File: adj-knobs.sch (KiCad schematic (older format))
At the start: 64 parts

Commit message: Initial PCB routed
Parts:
- removed C? (x2): 100nF, symbol Device:C_Small
- removed Q? (x4): 2N3904, Package_TO_SOT_THT:TO-92_Inline, symbol Transistor_BJT:2N3904
- removed U? (x14): 74HC14, symbol 74xx:74HC14
- added Q11, Q12, Q13, Q14: MMBT3904, Package_TO_SOT_SMD:SOT-23, symbol Transistor_BJT:MMBT3904
- added R70, R71, R72, R73: 1K, Resistor_SMD:R_0603_1608Metric_Pad0.98x0.95mm_HandSolder, symbol Device:R_Small
- added U1, U16, U17, U18, U19, U20: 74LVC2G14, Package_TO_SOT_SMD:SOT-23-6_Handsoldering, symbol 74xGxx:74LVC2G14
- C34, C35, C36, C37, C38, C39, C40, C41, C42, C43, C44, C45: renamed from C?; footprint (none) -> Capacitor_SMD:C_0603_1608Metric_Pad1.08x0.95mm_HandSolder
- R29, R30, R31, R32, R33, R35, R36, R37, R39, R40, R41, R43, R44, R45, R46, R47, R49, R50, R51, R52: renamed from R?; footprint (none) -> Resistor_SMD:R_0603_1608Metric_Pad0.98x0.95mm_HandSolder
- R34, R38, R42, R48: renamed from R?; value R_Small -> 1K; footprint (none) -> Resistor_SMD:R_0603_1608Metric_Pad0.98x0.95mm_HandSolder
- SW29, SW31, SW33, SW35: renamed from SW?; footprint (none) -> TL-1240:TL-1240
- SW30, SW32, SW34, SW36: renamed from SW?; footprint (none) -> Rotary_Encoder:RotaryEncoder_Alps_EC11E_Vertical_H20mm
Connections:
- wire segments 124 -> 120
- no-connect marks 8 -> 4

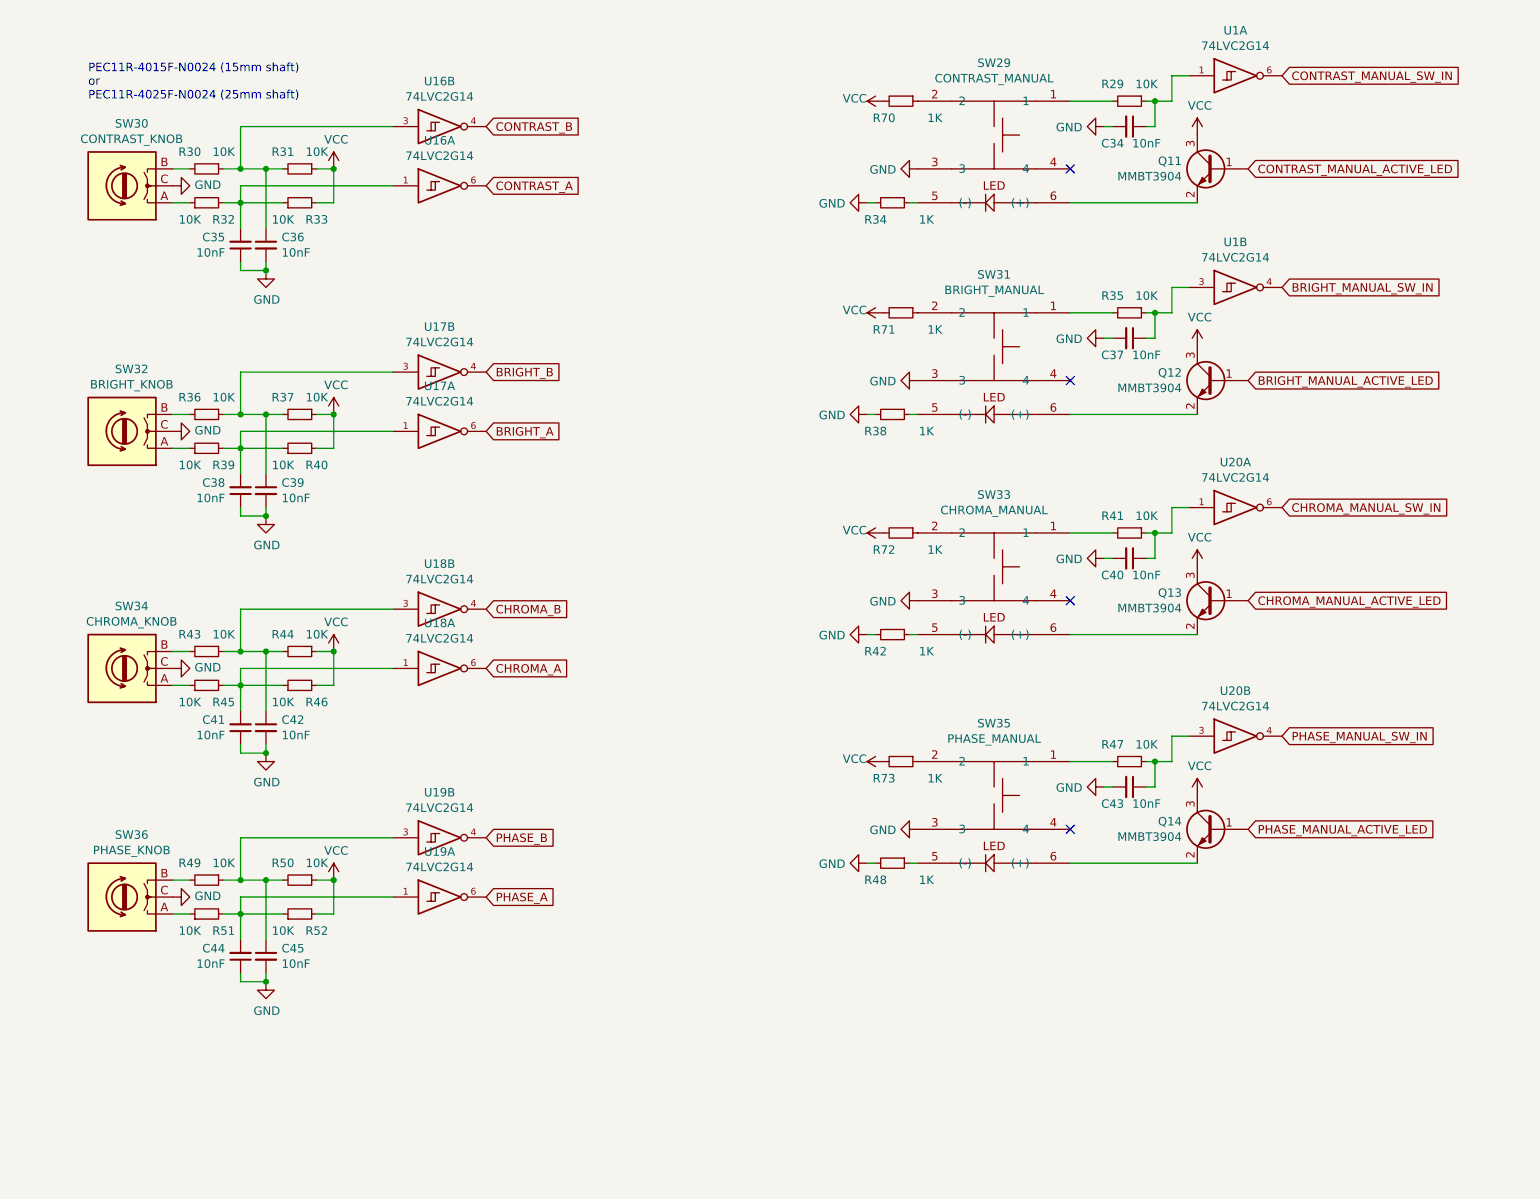
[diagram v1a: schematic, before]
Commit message: A bunch of changes, full duplex 422
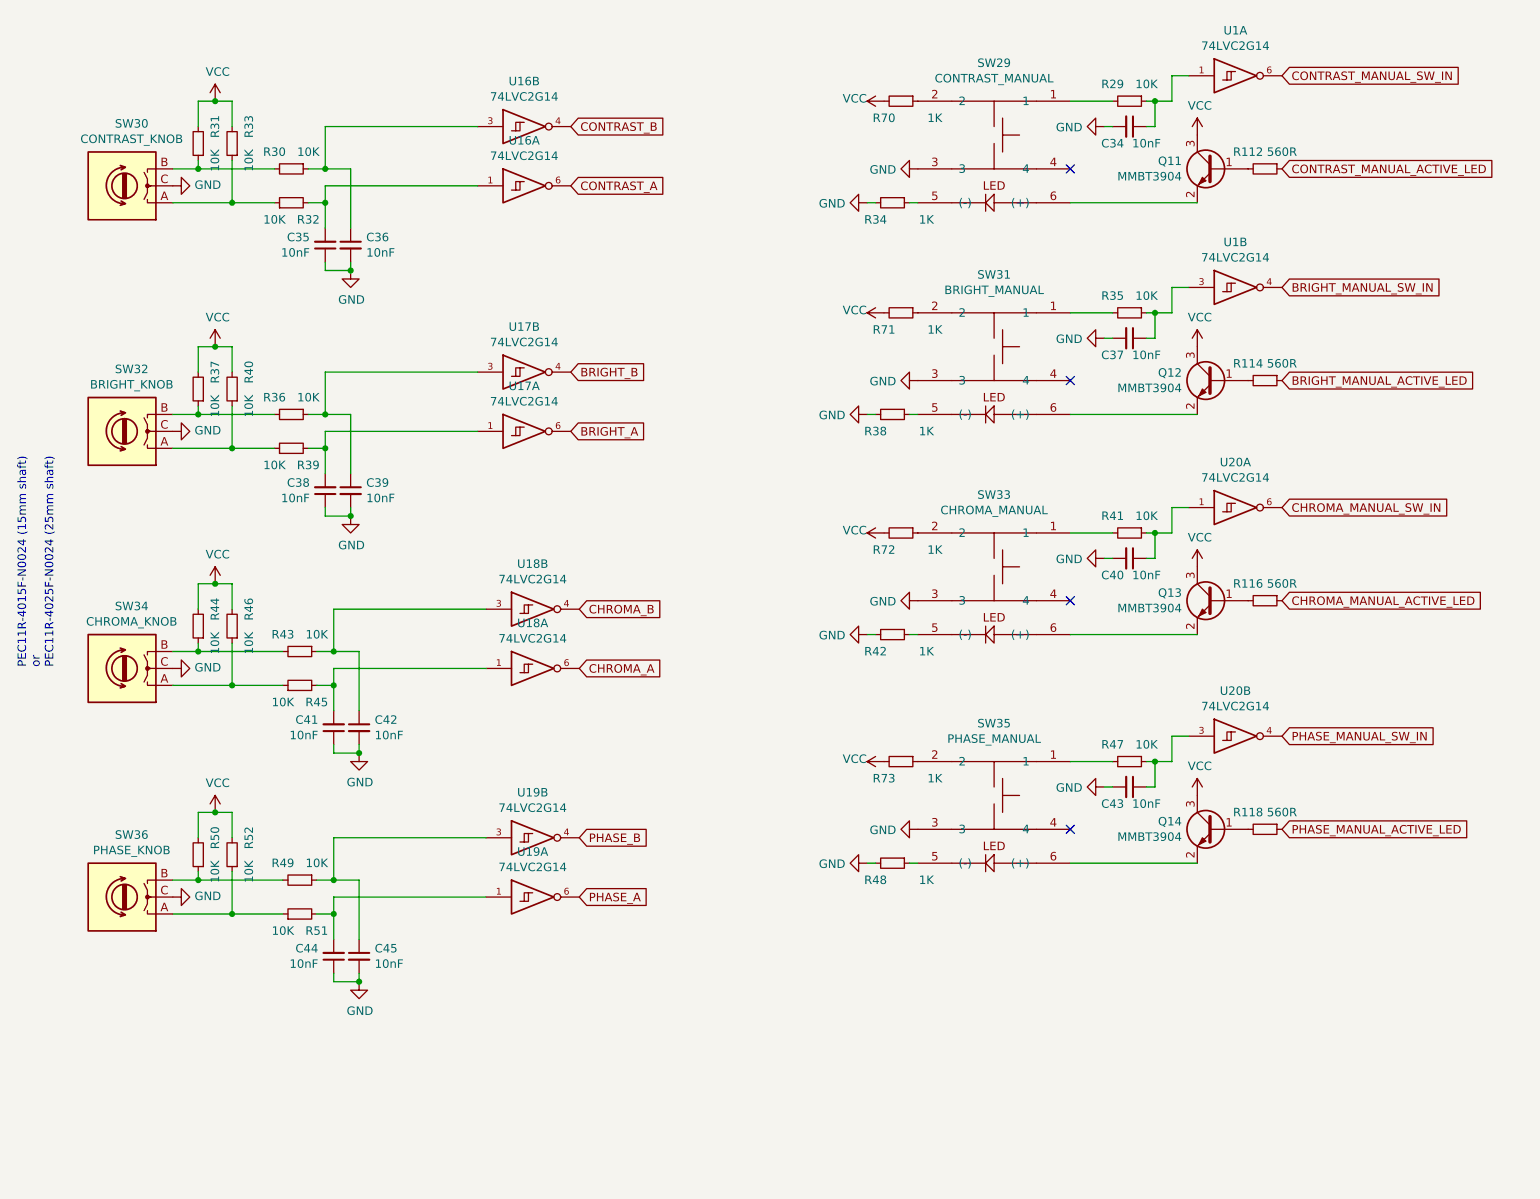
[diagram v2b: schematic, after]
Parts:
- added R112, R114, R116, R118: 560R, Resistor_SMD:R_0603_1608Metric_Pad0.98x0.95mm_HandSolder, symbol Device:R_Small
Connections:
- net BRIGHT_MANUAL_ACTIVE_LED: now also R114.1; no longer Q12.1 (B)
- net CHROMA_MANUAL_ACTIVE_LED: now also R116.1; no longer Q13.1 (B)
- net CONTRAST_MANUAL_ACTIVE_LED: now also R112.1; no longer Q11.1 (B)
- net PHASE_MANUAL_ACTIVE_LED: now also R118.1; no longer Q14.1 (B)
- net VCC: now also R31.2, R37.2, R44.2, R50.2; no longer R31.1, R37.1, R44.1, R50.1
- net at C45.1, R49.1, U19.3: no longer R50.2
- net at C44.2, R51.2, U19.1: no longer R52.1
- net at C42.1, R43.1, U18.3: no longer R44.2
- net at C41.2, R45.2, U18.1: no longer R46.1
- net at C39.1, R36.1, U17.3: no longer R37.2
- net at C38.2, R39.2, U17.1: no longer R40.1
- net at C36.1, R30.1, U16.3: no longer R31.2
- net at C35.2, R32.2, U16.1: no longer R33.1
- net at R32.1, SW30.A: now also R33.1
- net at R30.2, SW30.B: now also R31.1
- net at R39.1, SW32.A: now also R40.1
- net at R36.2, SW32.B: now also R37.1
- net at R45.1, SW34.A: now also R46.1
- net at R43.2, SW34.B: now also R44.1
- net at R51.1, SW36.A: now also R52.1
- net at R49.2, SW36.B: now also R50.1
- new net: Q11.1 (B), R112.2
- new net: Q12.1 (B), R114.2
- new net: Q13.1 (B), R116.2
- new net: Q14.1 (B), R118.2
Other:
- moved on the sheet: C35, C36, C38, C39, C41, C42, C44, C45, R30, R31, R32, R33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

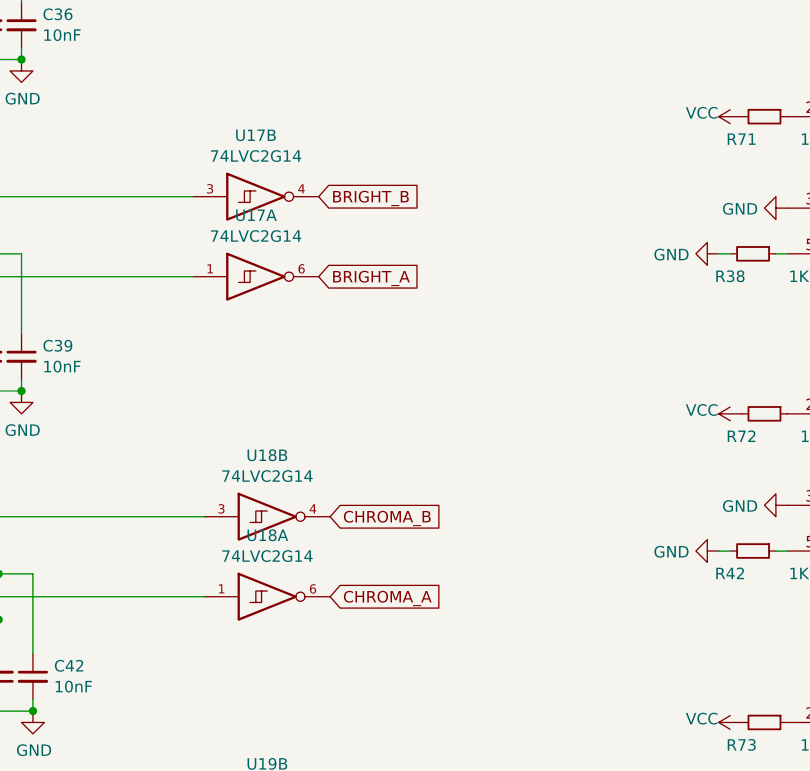
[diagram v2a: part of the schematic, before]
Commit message: Fixed switch footprints and encoder resistors
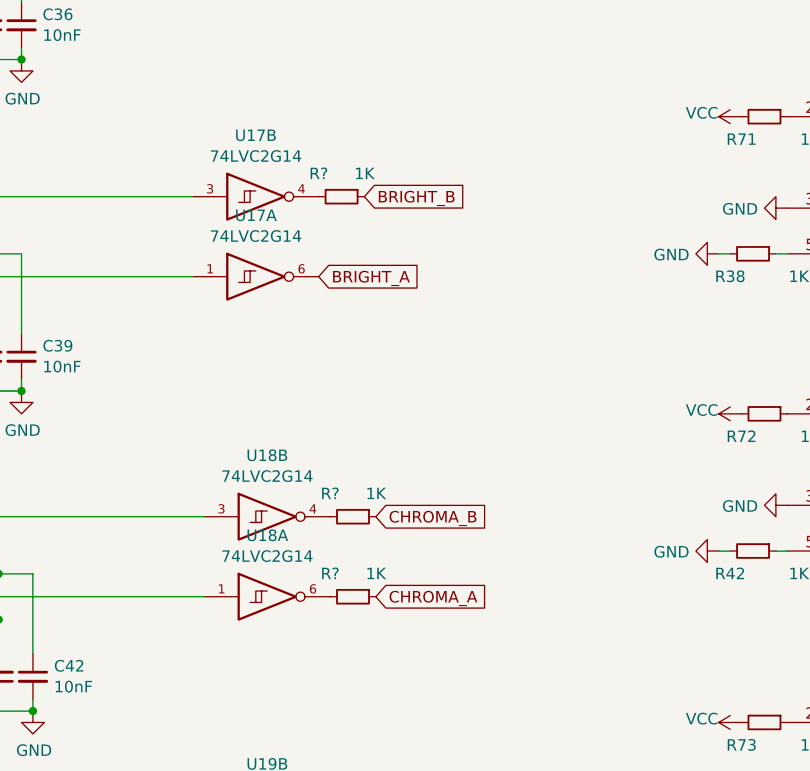
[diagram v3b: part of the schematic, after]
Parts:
- added R? (x3): 1K, Resistor_SMD:R_0603_1608Metric_Pad0.98x0.95mm_HandSolder, symbol Device:R_Small
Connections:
- net BRIGHT_B: now also R?.1; no longer U17.4
- net CHROMA_A: now also R?.1; no longer U18.6
- net CHROMA_B: now also R?.1; no longer U18.4
- new net: R?.2, U18.4
- new net: R?.2, U18.6
- new net: R?.2, U17.4
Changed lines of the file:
@@
 Text GLabel 4000 3200 2    50   Input ~ 0
 BRIGHT_A
-Text GLabel 4000 2850 2    50   Input ~ 0
+Text GLabel 4200 2850 2    50   Input ~ 0
 BRIGHT_B
 $Comp
@@
 Wire Wire Line
 	2600 4500 2750 4500
-Text GLabel 4050 4600 2    50   Input ~ 0
+Text GLabel 4250 4600 2    50   Input ~ 0
 CHROMA_A
-Text GLabel 4050 4250 2    50   Input ~ 0
+Text GLabel 4250 4250 2    50   Input ~ 0
 CHROMA_B
 $Comp
@@
 Wire Wire Line
 	1900 5450 2000 5450
+$Comp
+L Device:R_Small R?
+U 1 1 61CFAEB2
+P 4150 4250
+F 0 "R?" V 4050 4150 50  0000 C CNN
+F 1 "1K" V 4050 4350 50  0000 C CNN
+F 2 "Resistor_SMD:R_0603_1608Metric_Pad0.98x0.95mm_HandSolder" H 4150 4250 50  0001 C CNN
+F 3 "~" H 4150 4250 50  0001 C CNN
+	1    4150 4250
+	0    1    1    0
+$EndComp
+$Comp
+L Device:R_Small R?
+U 1 1 61D15885
+P 4150 4600
+F 0 "R?" V 4050 4500 50  0000 C CNN
+F 1 "1K" V 4050 4700 50  0000 C CNN
+F 2 "Resistor_SMD:R_0603_1608Metric_Pad0.98x0.95mm_HandSolder" H 4150 4600 50  0001 C CNN
+F 3 "~" H 4150 4600 50  0001 C CNN
+	1    4150 4600
+	0    1    1    0
+$EndComp
+$Comp
+L Device:R_Small R?
+U 1 1 61D279DB
+P 4100 2850
+F 0 "R?" V 4000 2750 50  0000 C CNN
+F 1 "1K" V 4000 2950 50  0000 C CNN
+F 2 "Resistor_SMD:R_0603_1608Metric_Pad0.98x0.95mm_HandSolder" H 4100 2850 50  0001 C CNN
+F 3 "~" H 4100 2850 50  0001 C CNN
+	1    4100 2850
+	0    1    1    0
+$EndComp
 $EndSCHEMATC

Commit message: 3D files and minor stuff
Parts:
- gave numbers to parts that had none: 3
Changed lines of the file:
@@
 encoding utf-8
 Sheet 5 6
-Title ""
+Title "BKM-10Rlternative"
 Date ""
 Rev ""
-Comp ""
+Comp "www.immerhax.com"
 Comment1 ""
 Comment2 ""
@@
 	1900 5450 2000 5450
 $Comp
-L Device:R_Small R?
+L Device:R_Small R113
 U 1 1 61CFAEB2
 P 4150 4250
-F 0 "R?" V 4050 4150 50  0000 C CNN
+F 0 "R113" V 4050 4150 50  0000 C CNN
 F 1 "1K" V 4050 4350 50  0000 C CNN
 F 2 "Resistor_SMD:R_0603_1608Metric_Pad0.98x0.95mm_HandSolder" H 4150 4250 50  0001 C CNN
@@
 $EndComp
 $Comp
-L Device:R_Small R?
+L Device:R_Small R115
 U 1 1 61D15885
 P 4150 4600
-F 0 "R?" V 4050 4500 50  0000 C CNN
+F 0 "R115" V 4050 4500 50  0000 C CNN
 F 1 "1K" V 4050 4700 50  0000 C CNN
 F 2 "Resistor_SMD:R_0603_1608Metric_Pad0.98x0.95mm_HandSolder" H 4150 4600 50  0001 C CNN
@@
 $EndComp
 $Comp
-L Device:R_Small R?
+L Device:R_Small R111
 U 1 1 61D279DB
 P 4100 2850
-F 0 "R?" V 4000 2750 50  0000 C CNN
+F 0 "R111" V 4000 2750 50  0000 C CNN
 F 1 "1K" V 4000 2950 50  0000 C CNN
 F 2 "Resistor_SMD:R_0603_1608Metric_Pad0.98x0.95mm_HandSolder" H 4100 2850 50  0001 C CNN

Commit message: Initial revision B
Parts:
- removed R111, R113, R115: 1K, Resistor_SMD:R_0603_1608Metric_Pad0.98x0.95mm_HandSolder, symbol Device:R_Small
- SW29, SW31, SW33, SW35: footprint TL-1240:TL-1240 -> TL-1265:TL-1265
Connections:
- net BRIGHT_B: now also U17.4
- net CHROMA_A: now also U18.6
- net CHROMA_B: now also U18.4
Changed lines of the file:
@@
 F 0 "SW29" H 6500 1975 50  0000 C CNN
 F 1 "CONTRAST_MANUAL" H 6500 1884 50  0000 C CNN
-F 2 "TL-1240:TL-1240" H 6500 1650 50  0001 C CNN
+F 2 "TL-1265:TL-1265" H 6500 1650 50  0001 C CNN
 F 3 "" H 6500 1650 50  0001 C CNN
 	1    6500 1500
@@
 F 0 "SW31" H 6500 3225 50  0000 C CNN
 F 1 "BRIGHT_MANUAL" H 6500 3134 50  0000 C CNN
-F 2 "TL-1240:TL-1240" H 6500 2900 50  0001 C CNN
+F 2 "TL-1265:TL-1265" H 6500 2900 50  0001 C CNN
 F 3 "" H 6500 2900 50  0001 C CNN
 	1    6500 2750
@@
 F 0 "SW33" H 6500 4525 50  0000 C CNN
 F 1 "CHROMA_MANUAL" H 6500 4434 50  0000 C CNN
-F 2 "TL-1240:TL-1240" H 6500 4200 50  0001 C CNN
+F 2 "TL-1265:TL-1265" H 6500 4200 50  0001 C CNN
 F 3 "" H 6500 4200 50  0001 C CNN
 	1    6500 4050
@@
 F 0 "SW35" H 6500 5875 50  0000 C CNN
 F 1 "PHASE_MANUAL" H 6500 5784 50  0000 C CNN
-F 2 "TL-1240:TL-1240" H 6500 5550 50  0001 C CNN
+F 2 "TL-1265:TL-1265" H 6500 5550 50  0001 C CNN
 F 3 "" H 6500 5550 50  0001 C CNN
 	1    6500 5400
@@
 Text GLabel 4000 3200 2    50   Input ~ 0
 BRIGHT_A
-Text GLabel 4200 2850 2    50   Input ~ 0
+Text GLabel 4000 2850 2    50   Input ~ 0
 BRIGHT_B
 $Comp
@@
 Wire Wire Line
 	2600 4500 2750 4500
-Text GLabel 4250 4600 2    50   Input ~ 0
+Text GLabel 4050 4600 2    50   Input ~ 0
 CHROMA_A
-Text GLabel 4250 4250 2    50   Input ~ 0
+Text GLabel 4050 4250 2    50   Input ~ 0
 CHROMA_B
 $Comp
@@
 Wire Wire Line
 	1900 5450 2000 5450
-$Comp
-L Device:R_Small R113
-U 1 1 61CFAEB2
-P 4150 4250
-F 0 "R113" V 4050 4150 50  0000 C CNN
-F 1 "1K" V 4050 4350 50  0000 C CNN
-F 2 "Resistor_SMD:R_0603_1608Metric_Pad0.98x0.95mm_HandSolder" H 4150 4250 50  0001 C CNN
-F 3 "~" H 4150 4250 50  0001 C CNN
-	1    4150 4250
-	0    1    1    0
-$EndComp
-$Comp
-L Device:R_Small R115
-U 1 1 61D15885
-P 4150 4600
-F 0 "R115" V 4050 4500 50  0000 C CNN
-F 1 "1K" V 4050 4700 50  0000 C CNN
-F 2 "Resistor_SMD:R_0603_1608Metric_Pad0.98x0.95mm_HandSolder" H 4150 4600 50  0001 C CNN
-F 3 "~" H 4150 4600 50  0001 C CNN
-	1    4150 4600
-	0    1    1    0
-$EndComp
-$Comp
-L Device:R_Small R111
-U 1 1 61D279DB
-P 4100 2850
-F 0 "R111" V 4000 2750 50  0000 C CNN
-F 1 "1K" V 4000 2950 50  0000 C CNN
-F 2 "Resistor_SMD:R_0603_1608Metric_Pad0.98x0.95mm_HandSolder" H 4100 2850 50  0001 C CNN
-F 3 "~" H 4100 2850 50  0001 C CNN
-	1    4100 2850
-	0    1    1    0
-$EndComp
 $EndSCHEMATC
